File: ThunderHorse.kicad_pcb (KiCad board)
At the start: 6 copper layers, 99.1 x 60 mm, 258 parts, among them J1 JTAG, J10 MOTOR1, J11 SWD1, J12 MOTOR1, J13 SWD1, J14 MOTOR1, J16 UFL, J17 IO1, J18 IO2, J2 HH-16P-CB-TYPE-C, J3 GPS, J4 CAM, J5 GPS, J6 CAM, J7 SWD1, J8 MOTOR1, J9 SWD1, Q1 XRS306D, Q10 XRS306D, Q11 XRS306D, Q12 XRS306D, Q13 SI2312BDS, Q2 XRS306D, Q3 XRS306D, Q4 XRS306D, Q5 XRS306D, Q6 XRS306D, Q7 XRS306D, Q8 XRS306D, Q9 XRS306D, SW1 TS2306A, SW2 TS2306A, U1 BATTERY, U10 STM32G071GBUxN, U11 DRV8300D, U12 STM32G071GBUxN, U13 DRV8300D, U14 STM32G071GBUxN, U15 DRV8300D, U16 TPRT9013-33, U17 ICM-42688-P, U18 BMP280, U19 INA230, U2 TPS63070RNMR, U20 TPRT9013-33, U21 SX1280IMLTRT, U22 AT2401C, U3 TPRT9013-33, U4 TPS2121, U5 RP2354B, U6 W25Q128JVPIQ, U7 USBLC6-2P6, U8 STM32G071GBUxN, U9 DRV8300D, Y1 40MHz, Y2 52MHz/10ppm

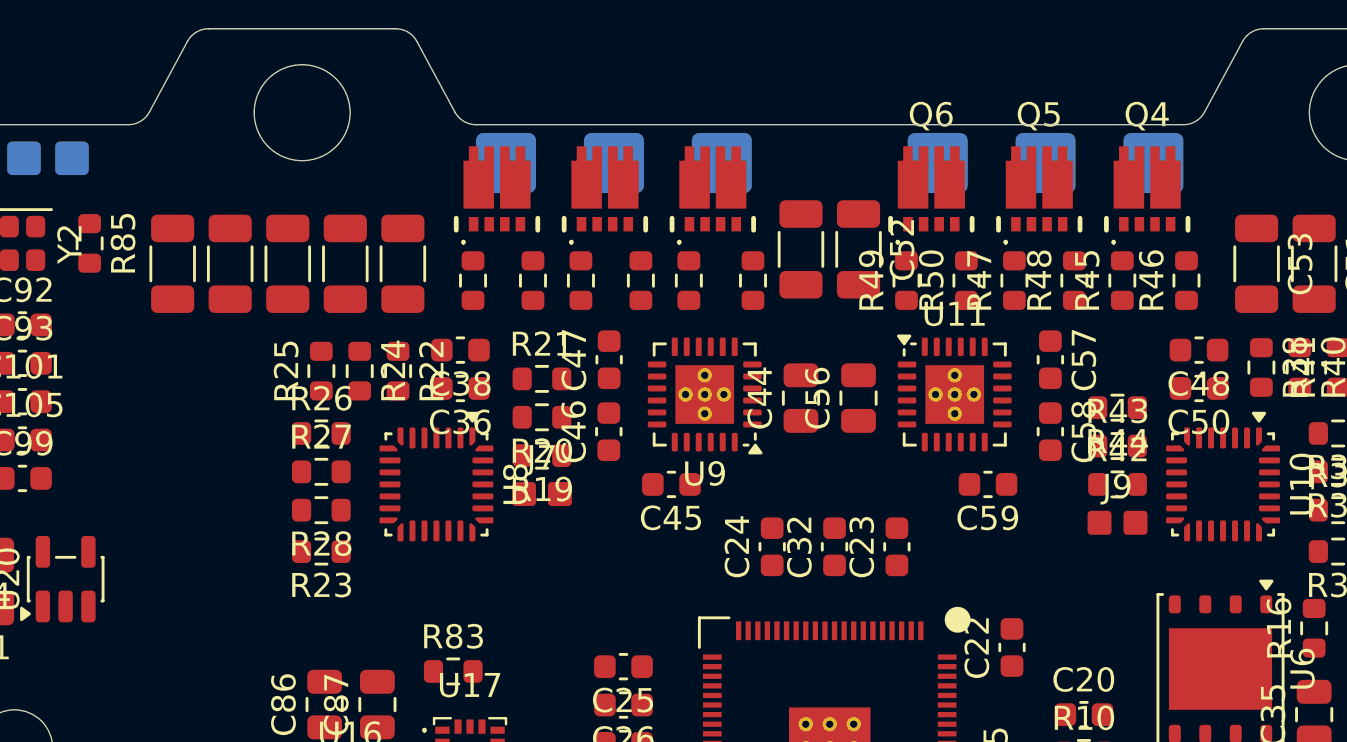
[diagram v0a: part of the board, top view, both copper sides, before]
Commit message: Settings and ESC layout
Updated the PCB configuration options for manufacturing.
Completed the initial ESC layout.

TODO:
Replicate ESC layout.
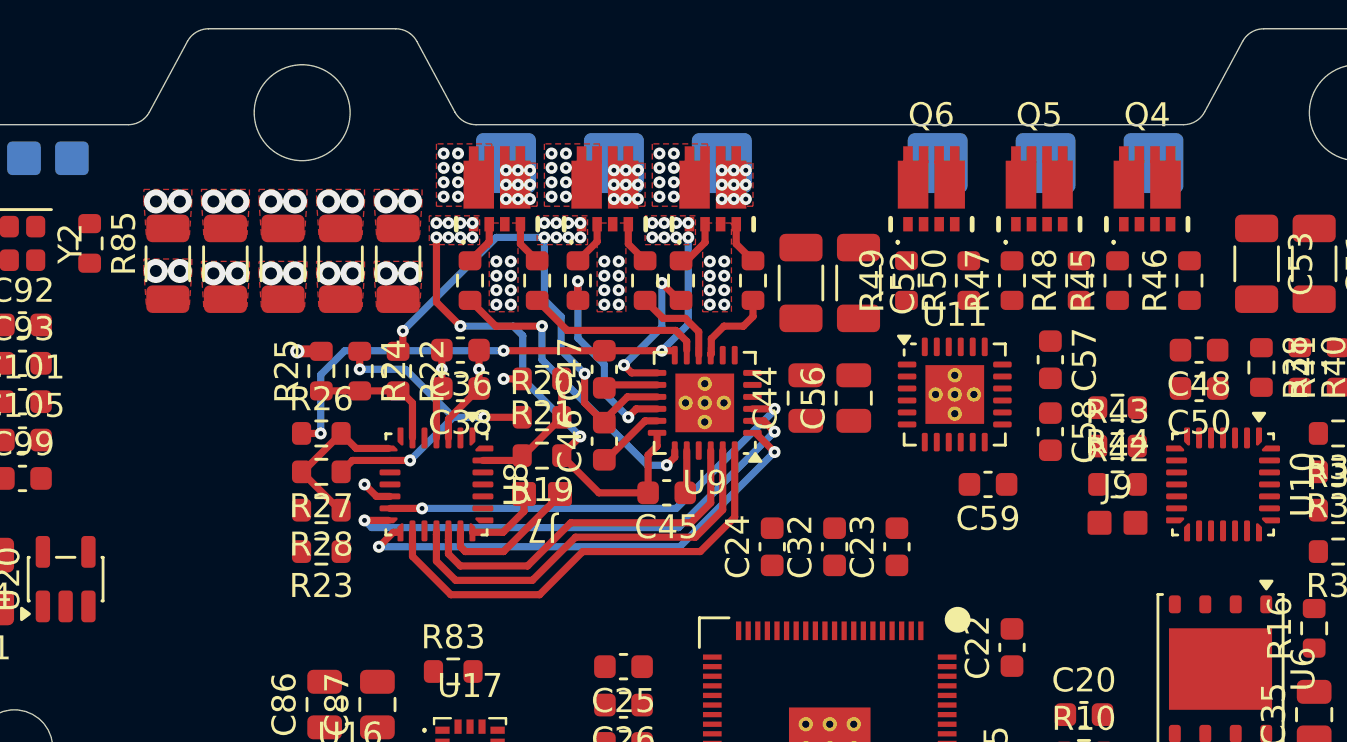
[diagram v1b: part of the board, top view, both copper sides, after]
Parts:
- J10, J12, J14, J8: footprint Custom_Parts:PAD_3_SQUARE_SOLID_2.5x2.5mm_P4.0mm -> Custom_Parts:PAD_3_SQUARE_SOLID_2.5x2.5mm_P4.0mm_MOTOR
- moved R34 9.18 mm to (136.8, 80.5)
- moved R29 9.12 mm to (125.0, 80.5)
- moved R30 9.00 mm to (127.8, 80.5)
- moved Q1 9.00 mm to (126.1, 77.5)
- moved Q3 9.00 mm to (135.1, 77.5)
- moved R33 8.68 mm to (133.8, 80.5)
- moved C36 1.60 mm to (124.6, 83.4)
- moved C38 1.60 mm to (124.6, 85.0)
- moved C41 1.40 mm to (138.8, 80.6)
- moved C52 1.40 mm to (141.2, 80.6)
- moved C47 0.45 mm to (130.6, 84.2)
- moved C46 0.44 mm to (130.6, 87.2)
- moved C45 0.40 mm to (133.2, 89.3)
- moved U9 0.35 mm to (134.8, 85.6)
- moved R48 0.20 mm to (150.4, 80.5)
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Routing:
- net /ESC/ESC1/MOTOR_C: track 0.00 -> 23.4 mm, vias 0 -> 20
- net /ESC/ESC1/B_LOW: track 0.00 -> 21.0 mm, vias 0 -> 2
- net /ESC/ESC1/A_LOW: track 0.00 -> 20.2 mm, vias 0 -> 2
- net /ESC/ESC1/MOTOR_A: track 0.00 -> 20.0 mm, vias 0 -> 19
- net /ESC/ESC1/MOTOR_B: track 0.00 -> 19.9 mm, vias 0 -> 19
- net /ESC/ESC1/C_HIGH: track 0.00 -> 19.3 mm
- net /ESC/ESC1/C_LOW: track 0.00 -> 18.7 mm, vias 0 -> 2
- net /ESC/ESC1/B_HIGH: track 0.00 -> 17.2 mm
- net /ESC/ESC1/A_HIGH: track 0.00 -> 15.4 mm
- net /ESC/ESC1/BEMF_REF: track 0.00 -> 14.0 mm, vias 0 -> 3
- net /ESC/ESC1/GHA: track 0.00 -> 12.6 mm, vias 0 -> 2
- net /ESC/ESC1/GHB: track 0.00 -> 8.70 mm, vias 0 -> 2
- net /ESC/ESC1/GLA: track 0.00 -> 7.31 mm
- net /ESC/ESC1/BEMF_C: track 0.00 -> 6.86 mm
- net /ESC/ESC1/GHC: track 0.00 -> 6.70 mm, vias 0 -> 2
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- added copper zone on F.Cu, net /ESC/ESC1/MOTOR_A
- added copper zone on In2.Cu, net /ESC/ESC1/MOTOR_A
- added copper zone on F.Cu, net /ESC/ESC1/MOTOR_B
- added copper zone on In2.Cu, net /ESC/ESC1/MOTOR_B
- added copper zone on F.Cu, net /ESC/ESC1/MOTOR_C
- added copper zone on In2.Cu, net /ESC/ESC1/MOTOR_C
- added copper zone on F.Cu, net GND

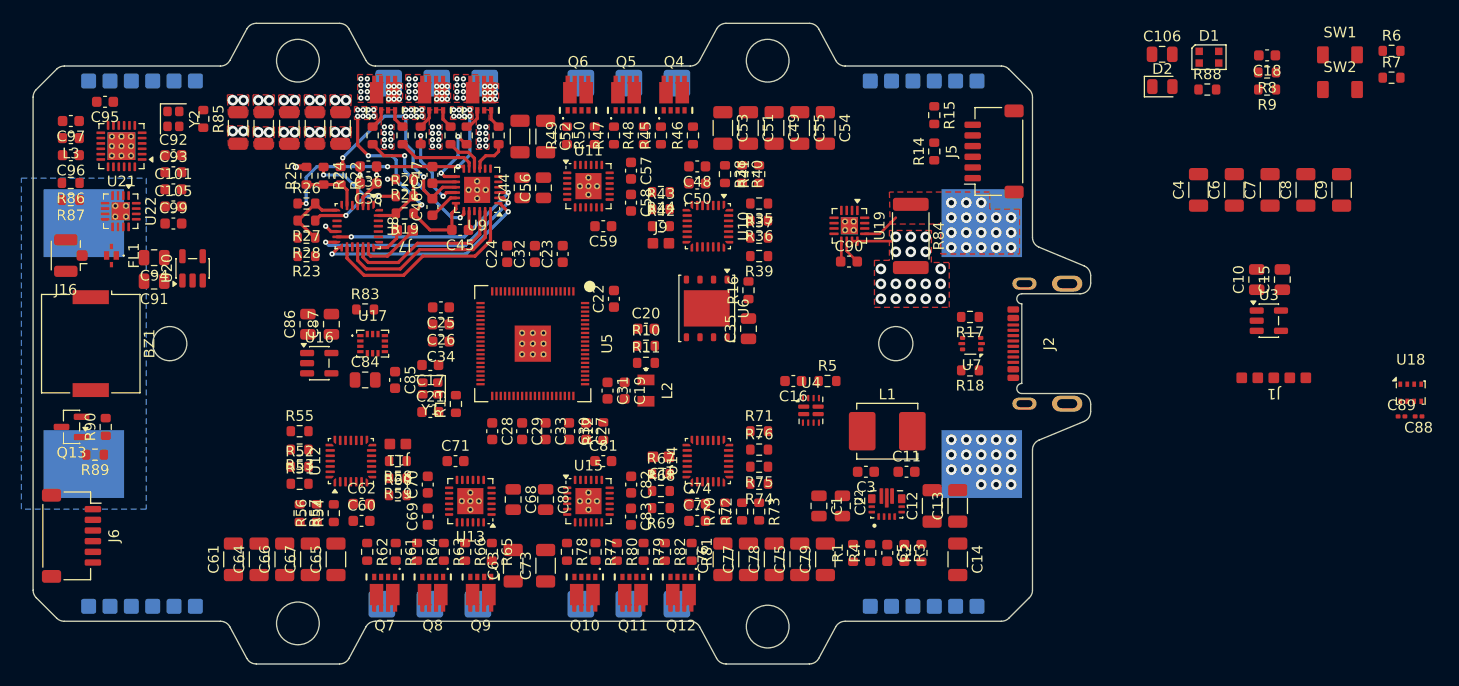
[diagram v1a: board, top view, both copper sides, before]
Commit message: License and ESC layout
Added a file extension to the license.
Updated the second ESC layout.

TODO:
Continue the ESC layout.
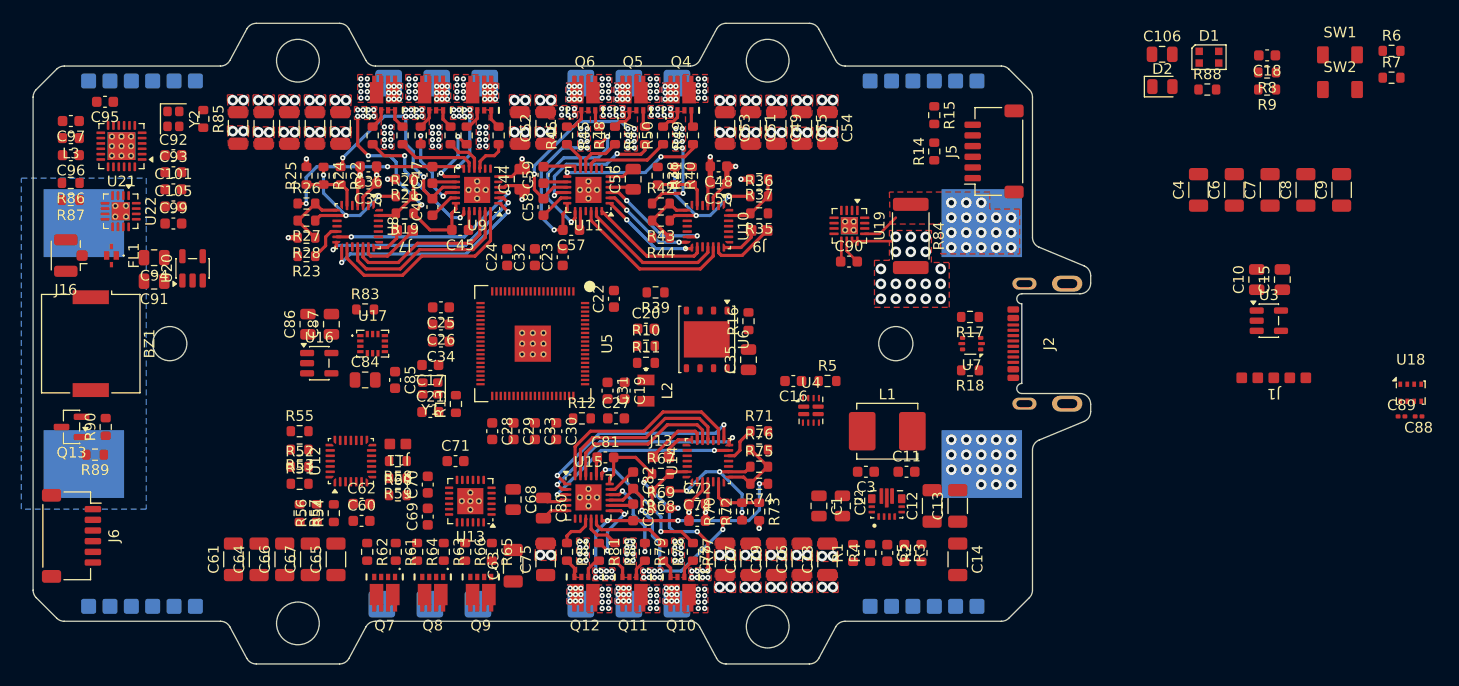
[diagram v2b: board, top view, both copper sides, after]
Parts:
- moved C73 26.4 mm to (167.6, 120.2)
- moved C75 23.8 mm to (141.2, 120.2)
- moved R46 11.8 mm to (143.2, 80.5)
- moved R49 11.8 mm to (155.0, 80.5)
- moved R39 10.3 mm to (151.5, 95.2)
- moved J9 9.28 mm to (161.2, 89.4), turned to 180 degrees
- moved R82 9.18 mm to (143.2, 119.5)
- moved R77 9.12 mm to (155.0, 119.5)
- moved Q10 9.00 mm to (153.9, 122.5)
- moved Q12 9.00 mm to (144.9, 122.5)
- moved R78 9.00 mm to (152.2, 119.5)
- moved R81 8.68 mm to (146.2, 119.5)
- moved C56 8.44 mm to (149.4, 84.6)
- moved C58 8.21 mm to (141.0, 87.2), turned to 90 degrees
- moved C57 7.88 mm to (143.6, 89.3), turned to 180 degrees
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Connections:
- J10 pad 1: /ESC/ESC2/MOTOR_A -> /ESC/ESC2/MOTOR_C
- J10 pad 3: /ESC/ESC2/MOTOR_C -> /ESC/ESC2/MOTOR_A
- Q4 pad 1: /ESC/ESC2/MOTOR_A -> GND
- Q4 pad 2: /ESC/ESC2/GHA_IN -> /ESC/ESC2/GLC_IN
- Q4 pad 3: GND -> /ESC/ESC2/MOTOR_C
- Q4 pad 4: /ESC/ESC2/GLA_IN -> /ESC/ESC2/GHC_IN
- Q4 pad 5: /ESC/ESC2/MOTOR_A -> VBAT
- Q4 pad 6: VBAT -> /ESC/ESC2/MOTOR_C
- Q5 pad 1: /ESC/ESC2/MOTOR_B -> GND
- Q5 pad 2: /ESC/ESC2/GHB_IN -> /ESC/ESC2/GLB_IN
- Q5 pad 3: GND -> /ESC/ESC2/MOTOR_B
- Q5 pad 4: /ESC/ESC2/GLB_IN -> /ESC/ESC2/GHB_IN
- Q5 pad 5: /ESC/ESC2/MOTOR_B -> VBAT
- Q5 pad 6: VBAT -> /ESC/ESC2/MOTOR_B
- Q6 pad 1: /ESC/ESC2/MOTOR_C -> GND
- Q6 pad 2: /ESC/ESC2/GHC_IN -> /ESC/ESC2/GLA_IN
- Q6 pad 3: GND -> /ESC/ESC2/MOTOR_A
- Q6 pad 4: /ESC/ESC2/GLC_IN -> /ESC/ESC2/GHA_IN
- Q6 pad 5: /ESC/ESC2/MOTOR_C -> VBAT
- Q6 pad 6: VBAT -> /ESC/ESC2/MOTOR_A
- Q7 pad 1: /ESC/ESC3/MOTOR_A -> GND
- Q7 pad 2: /ESC/ESC3/GHA_IN -> /ESC/ESC3/GLA_IN
- Q7 pad 3: GND -> /ESC/ESC3/MOTOR_A
- Q7 pad 4: /ESC/ESC3/GLA_IN -> /ESC/ESC3/GHA_IN
- Q7 pad 5: /ESC/ESC3/MOTOR_A -> VBAT
- Q7 pad 6: VBAT -> /ESC/ESC3/MOTOR_A
- Q8 pad 1: /ESC/ESC3/MOTOR_B -> GND
- Q8 pad 2: /ESC/ESC3/GHB_IN -> /ESC/ESC3/GLB_IN
- Q8 pad 3: GND -> /ESC/ESC3/MOTOR_B
- Q8 pad 4: /ESC/ESC3/GLB_IN -> /ESC/ESC3/GHB_IN
- Q8 pad 5: /ESC/ESC3/MOTOR_B -> VBAT
- Q8 pad 6: VBAT -> /ESC/ESC3/MOTOR_B
- Q9 pad 1: /ESC/ESC3/MOTOR_C -> GND
- Q9 pad 2: /ESC/ESC3/GHC_IN -> /ESC/ESC3/GLC_IN
- Q9 pad 3: GND -> /ESC/ESC3/MOTOR_C
- Q9 pad 4: /ESC/ESC3/GLC_IN -> /ESC/ESC3/GHC_IN
- Q9 pad 5: /ESC/ESC3/MOTOR_C -> VBAT
- Q9 pad 6: VBAT -> /ESC/ESC3/MOTOR_C
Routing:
- net /ESC/ESC4/MOTOR_C: track 0.00 -> 23.4 mm, vias 0 -> 20
- net /ESC/ESC4/B_LOW: track 0.00 -> 20.2 mm, vias 0 -> 2
- net /ESC/ESC4/A_LOW: track 0.00 -> 20.0 mm, vias 0 -> 2
- net /ESC/ESC4/MOTOR_A: track 0.00 -> 20.0 mm, vias 0 -> 19
- net /ESC/ESC4/MOTOR_B: track 0.00 -> 19.9 mm, vias 0 -> 19
- net GND: track 7.58 -> 27.5 mm, vias 55 -> 134
- net /ESC/ESC4/C_HIGH: track 0.00 -> 19.3 mm
- net /ESC/ESC4/C_LOW: track 0.00 -> 18.7 mm, vias 0 -> 2
- net /ESC/ESC4/B_HIGH: track 0.00 -> 17.2 mm
- net /ESC/ESC2/MOTOR_B: track 0.00 -> 16.9 mm, vias 0 -> 18
- net /ESC/ESC2/A_HIGH: track 0.00 -> 15.6 mm
- net /ESC/ESC4/A_HIGH: track 0.00 -> 15.4 mm
- net /ESC/ESC2/GHA: track 0.00 -> 15.4 mm, vias 0 -> 2
- net /ESC/ESC2/MOTOR_A: track 0.00 -> 14.2 mm, vias 0 -> 18
- net /ESC/ESC4/BEMF_REF: track 0.00 -> 13.9 mm, vias 0 -> 3
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- added copper zone on B.Cu, net /ESC/ESC1/MOTOR_A
- added copper zone on B.Cu, net /ESC/ESC1/MOTOR_B
- added copper zone on B.Cu, net /ESC/ESC1/MOTOR_C
- added copper zone on B.Cu, net /ESC/ESC2/MOTOR_A
- added copper zone on F.Cu, net /ESC/ESC2/MOTOR_A
- added copper zone on In2.Cu, net /ESC/ESC2/MOTOR_A
- added copper zone on B.Cu, net /ESC/ESC2/MOTOR_B
- added copper zone on F.Cu, net /ESC/ESC2/MOTOR_B
- added copper zone on In2.Cu, net /ESC/ESC2/MOTOR_B
- added copper zone on B.Cu, net /ESC/ESC2/MOTOR_C
- added copper zone on F.Cu, net /ESC/ESC2/MOTOR_C
- added copper zone on In2.Cu, net /ESC/ESC2/MOTOR_C
- added copper zone on B.Cu, net /ESC/ESC4/MOTOR_A
- added copper zone on F.Cu, net /ESC/ESC4/MOTOR_A
- added copper zone on In2.Cu, net /ESC/ESC4/MOTOR_A
- added copper zone on B.Cu, net /ESC/ESC4/MOTOR_B
- added copper zone on F.Cu, net /ESC/ESC4/MOTOR_B
- added copper zone on In2.Cu, net /ESC/ESC4/MOTOR_B
- added copper zone on B.Cu, net /ESC/ESC4/MOTOR_C
- added copper zone on F.Cu, net /ESC/ESC4/MOTOR_C
- added copper zone on In2.Cu, net /ESC/ESC4/MOTOR_C
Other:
- board text added: "ESC REFERENCES"

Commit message: ESC layout
Updated the layout for the final ESC.
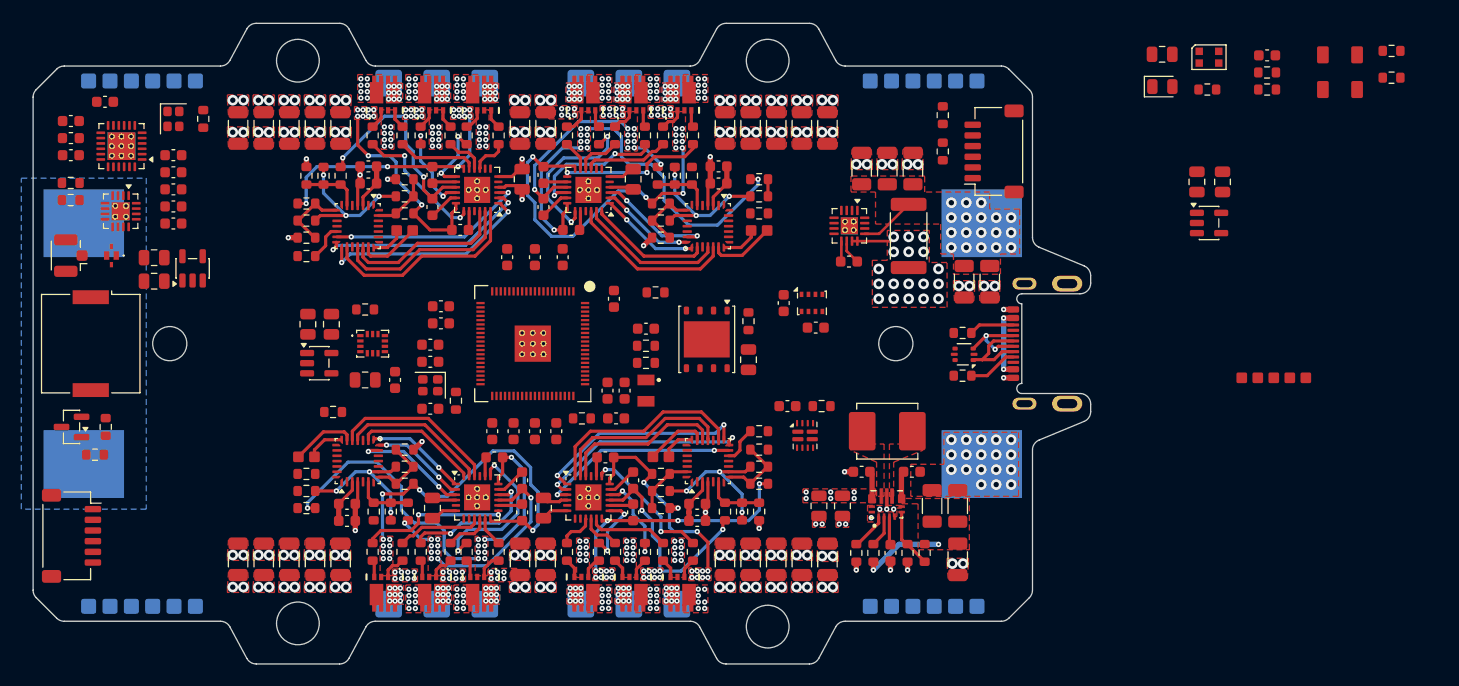
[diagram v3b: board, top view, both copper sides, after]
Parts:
- C88, C89: footprint Capacitor_SMD:C_0201_0603Metric -> Capacitor_SMD:C_0603_1608Metric
- U18: footprint Package_LGA:Bosch_LGA-8_2x2.5mm_P0.65mm_ClockwisePinNumbering -> Custom_Parts:LGA-8_2x2.5mm_P0.65mm
- moved C89 58.8 mm to (163.5, 96.2), turned to 90 degrees
- moved C88 57.1 mm to (166.5, 98.5)
- moved U18 56.7 mm to (166.1, 96.2)
- moved C7 38.3 mm to (170.8, 83.6)
- moved C9 34.1 mm to (182.8, 94.2), turned to -90 degrees
- moved C8 33.1 mm to (180.4, 94.2), turned to -90 degrees
- moved C6 30.2 mm to (175.6, 83.6)
- moved C4 29.2 mm to (173.2, 83.6)
- moved C61 26.8 mm to (138.8, 120.2), turned to -90 degrees
- moved C63 18.6 mm to (119.6, 120.2)
- moved R62 12.3 mm to (136.8, 119.5)
- moved R65 11.2 mm to (125.0, 119.5)
- moved C10 10.7 mm to (202.2, 84.8)
- moved C15 10.7 mm to (204.6, 84.8)
- moved U3 10.7 mm to (203.3, 88.7)
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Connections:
- J10 pad 1: /ESC/ESC2/MOTOR_C -> /ESC/ESC2/MOTOR_A
- J10 pad 3: /ESC/ESC2/MOTOR_A -> /ESC/ESC2/MOTOR_C
- R55 pad 2: ESC3 -> ESC2
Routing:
- net /ESC/ESC3/MOTOR_A: track 0.00 -> 39.1 mm, vias 0 -> 19
- net /ESC/ESC3/MOTOR_C: track 0.00 -> 32.1 mm, vias 0 -> 20
- net /ESC/ESC2/MOTOR_A: track 14.2 -> 39.1 mm, vias 18 -> 19
- net /ESC/ESC2/MOTOR_C: track 10.5 -> 32.1 mm, vias 18 -> 20
- net /ESC/ESC3/MOTOR_B: track 0.00 -> 20.4 mm, vias 0 -> 19
- net /ESC/ESC3/A_HIGH: track 0.00 -> 15.7 mm
- net /ESC/ESC3/GHA: track 0.00 -> 15.4 mm, vias 0 -> 2
- net /ESC/ESC3/GHC: track 0.00 -> 13.9 mm, vias 0 -> 2
- net /ESC/ESC3/BEMF_REF: track 0.00 -> 13.9 mm, vias 0 -> 3
- net /ESC/ESC3/B_HIGH: track 0.00 -> 13.7 mm
- net /ESC/ESC3/GHB: track 0.00 -> 13.2 mm, vias 0 -> 2
- net GND: track 27.5 -> 40.2 mm, vias 134 -> 195
- net /ESC/ESC3/C_HIGH: track 0.00 -> 11.5 mm
- net /ESC/ESC3/C_LOW: track 0.00 -> 10.9 mm, vias 0 -> 2
- net 5V_REG: track 0.00 -> 10.1 mm, vias 0 -> 2
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- added copper zone on B.Cu, net /ESC/ESC3/MOTOR_A
- added copper zone on F.Cu, net /ESC/ESC3/MOTOR_A
- added copper zone on In2.Cu, net /ESC/ESC3/MOTOR_A
- added copper zone on B.Cu, net /ESC/ESC3/MOTOR_B
- added copper zone on F.Cu, net /ESC/ESC3/MOTOR_B
- added copper zone on In2.Cu, net /ESC/ESC3/MOTOR_B
- added copper zone on B.Cu, net /ESC/ESC3/MOTOR_C
- added copper zone on F.Cu, net /ESC/ESC3/MOTOR_C
- added copper zone on In2.Cu, net /ESC/ESC3/MOTOR_C
- added copper zone on F.Cu, net /Power/L1
- added copper zone on F.Cu, net /Power/L2
- added copper zone on F.Cu, net 5V_REG

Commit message: MCU layout
Started the MCU layout.

TODO:
Check the previous iterations.
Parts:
- added R91: 5.1K, Resistor_SMD:R_0603_1608Metric, F.Cu at (167.0, 87.4)
- added R92: 5.1K, Resistor_SMD:R_0603_1608Metric, F.Cu at (165.4, 87.4)
- moved R6 115.5 mm to (111.2, 110.0), turned to 180 degrees
- moved R7 114.2 mm to (111.2, 108.4), turned to 180 degrees
- moved SW1 111.5 mm to (111.2, 112.0)
- moved SW2 111.2 mm to (111.2, 114.6)
- moved R39 45.1 mm to (193.0, 77.4)
- moved C15 40.9 mm to (165.9, 98.1), turned to -90 degrees
- moved C10 37.2 mm to (168.8, 101.3), turned to 0 degrees
- moved U3 35.8 mm to (168.8, 98.1), turned to 90 degrees
- moved J1 23.1 mm to (204.7, 80.6)
- moved C34 5.56 mm to (131.2, 105.6)
- moved R16 4.48 mm to (161.2, 102.3), turned to 180 degrees
- moved C88 4.19 mm to (166.6, 94.3)
- moved C89 4.19 mm to (163.6, 92.0)
- moved U18 4.19 mm to (166.2, 92.0)
- moved C17 3.79 mm to (131.2, 98.0)
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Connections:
- U4 pad 2: VBUS -> 5V_REG
- U4 pad 7: 5V_REG -> VBUS
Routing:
- net 3V3: track 18.7 -> 95.4 mm, vias 0 -> 25
- net GND: track 40.2 -> 85.6 mm, vias 195 -> 237
- net /MCU/USBT_D+: track 0.00 -> 31.4 mm
- net /MCU/USBT_D-: track 0.00 -> 30.4 mm
- net 1V1: track 0.00 -> 29.0 mm, vias 0 -> 8
- net /MCU/QSPI_SD1: track 0.00 -> 24.1 mm
- net /MCU/FLASH_SS: track 0.00 -> 21.5 mm, vias 0 -> 2
- net /MCU/QSPI_SD2: track 0.00 -> 21.5 mm
- net /MCU/QSPI_SD3: track 0.00 -> 13.1 mm
- net /MCU/QSPI_SCLK: track 0.00 -> 13.0 mm
- net /MCU/QSPI_SD0: track 0.00 -> 12.8 mm
- net 5V_REG: track 10.1 -> 0.78 mm, vias 2 -> 15
- net SENS_SDA: track 0.00 -> 7.58 mm
- net 5V: track 10.4 -> 17.4 mm, vias 1 -> 19
- net /MCU/XOUT: track 0.00 -> 6.93 mm
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- added copper zone on F.Cu, net /MCU/VREG_LX
- added copper zone on F.Cu, net 1V1
- added copper zone on F.Cu, net 3V3
- added copper zone on In2.Cu, net 3V3
- added copper zone on F.Cu, net 5V
- added copper zone on In2.Cu, net 5V_REG
- added copper zone on F.Cu, net VBUS
- added copper zone on In2.Cu, net VBUS
